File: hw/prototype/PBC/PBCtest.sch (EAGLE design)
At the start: 180 parts, among them IC1 7812L, U1 TC4427EOA, U10 TC4427EOA, U11 TC4427EOA, U12 TC4427EOA, U13 TC4427EOA, U14 TC4427EOA, U15 TC4427EOA, U16 TC4427EOA, U17 TC4427EOA, U18 TC4427EOA, U19 TC4427EOA, U2 TC4427EOA, U20 TC4427EOA, U21 TC4427EOA, U22 TC4427EOA, U23 TC4427EOA, U24 TC4427EOA, U25 TC4427EOA, U26 TC4427EOA, U27 TC4427EOA, U28 TC4427EOA, U29 TC4427EOA, U3 TC4427EOA, U30 TC4427EOA, U31 TC4427EOA, U32 TC4427EOA, U4 TC4427EOA, U5 TC4427EOA, U6 TC4427EOA, U7 TC4427EOA, U8 TC4427EOA, U9 TC4427EOA

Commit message: schematic done
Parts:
- removed C10, C11, C12, C13, C14, C15, C16, C17, C18, C19, C2, C20, C21, C22, C23, C24, C25, C26, C27, C28, C29, C3, C30, C31, C32, C34, C35, C36, C37, C38, C39, C4, C40, C41, C42, C43, C44, C45, C46, C47, C48, C49, C5, C50, C51, C52, C53, C54, C55, C56, C57, C58, C59, C6, C60, C61, C62, C63, C64, C7, C8, C9: 2.2uF, rcl:C-EUC1206
- removed RESET: (no value), switch-omron:10-XX
- removed SVI1, SVI2, SVI5, SVI6, SVO1, SVO2, SVO4, SVO5, SVO6: (no value), con-lstb:MA08-1
- removed SVI3, SVO3: (no value), con-lstb:MA10-1
- removed SVI7: (no value), con-lstb:MA18-2
- removed U$1, U$10, U$11, U$12, U$13, U$14, U$15, U$16, U$17, U$18, U$19, U$2, U$20, U$21, U$22, U$23, U$24, U$25, U$26, U$27, U$28, U$29, U$30, U$31, U$32, U$33, U$34, U$35, U$36, U$37, U$38, U$39, U$40, U$41, U$42, U$43, U$44, U$45, U$46, U$47, U$48, U$49, U$5, U$50, U$51, U$52, U$53, U$54, U$55, U$56, U$57, U$58, U$59, U$6, U$60, U$61, U$62, U$63, U$64, U$7, U$8, U$9: (no value), ultrasonic:TCT40-16
- removed U10, U11, U12, U13, U14, U15, U16, U17, U18, U19, U2, U20, U21, U22, U23, U24, U25, U26, U27, U28, U29, U3, U30, U31, U32, U4, U5, U6, U7, U8, U9: TC4427EOA, TC4427EOA:TC4427EOA
- added S1: (no value), switch-omron:10-XX
- C65, C66: value 100pF -> (none)
- D1: value 1N4001 -> 1N4004
- renumbered PWR_IN to J1, SVI4 to SVI10, VIN_ENABLE to SVJ8
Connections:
- removed net +18V: C1.1, C10.1, C11.1, C12.1, C13.1, C14.1, C15.1, C16.1, C17.1, C18.1, C19.1, C2.1, C20.1, C21.1, C22.1, C23.1, C24.1, C25.1, C26.1, C27.1, C28.1, C29.1, C3.1, C30.1, C31.1, C32.1, C33.1, C34.1, C35.1, C36.1, C37.1, C38.1, C39.1, C4.1, C40.1, C41.1, C42.1, C43.1, C44.1, C45.1, C46.1, C47.1, C48.1, C49.1, C5.1, C50.1, C51.1, C52.1, C53.1, C54.1, C55.1, C56.1, C57.1, C58.1, C59.1, C6.1, C60.1, C61.1, C62.1, C63.1, C64.1, C65.1, C7.1, C8.1, C9.1, D1.C, IC1.VI, U1.VDD, U10.VDD, U11.VDD, U12.VDD, U13.VDD, U14.VDD, U15.VDD, U16.VDD, U17.VDD, U18.VDD, U19.VDD, U2.VDD, U20.VDD, U21.VDD, U22.VDD, U23.VDD, U24.VDD, U25.VDD, U26.VDD, U27.VDD, U28.VDD, U29.VDD, U3.VDD, U30.VDD, U31.VDD, U32.VDD, U4.VDD, U5.VDD, U6.VDD, U7.VDD, U8.VDD, U9.VDD
- removed net +3V3: SVI10.5, SVO4.5
- removed net +5V: SVI10.4, SVI7.1, SVI7.2, SVO4.4
- removed net AREF: SVI3.8, SVO3.8
- removed net IOREF: SVI10.7, SVO4.7
- removed net PA0: SVI2.1, SVO2.1
- removed net PA1: SVI2.2, SVO2.2
- removed net PA10: SVI3.3, SVO3.3, U3.IN_A
- removed net PA11: SVI3.4, SVO3.4, U3.IN_B
- removed net PA12: SVI3.5, SVO3.5, U4.IN_A
- removed net PA13: SVI3.6, SVO3.6, U4.IN_B
- removed net PA14: SVI1.8, SVO1.8, U5.IN_A
- removed net PA15: SVI1.7, SVO1.7, U5.IN_B
- removed net PA16: SVI1.6, SVO1.6, U6.IN_A
- removed net PA17: SVI1.5, SVO1.5, U6.IN_B
- removed net PA18: SVI1.4, SVO1.4, U7.IN_A
- removed net PA19: SVI1.3, SVO1.3, U7.IN_B
- removed net PA2: SVI2.3, SVO2.3
- removed net PA20: SVI1.2, SVO1.2, U8.IN_A
- removed net PA21: SVI1.1, SVO1.1, U8.IN_B
- removed net PA22: SVI7.3, U9.IN_A
- removed net PA23: SVI7.4, U10.IN_A
- removed net PA24: SVI7.5, U9.IN_B
- removed net PA25: SVI7.6, U10.IN_B
- removed net PA26: SVI7.7, U11.IN_A
- removed net PA27: SVI7.8, U12.IN_A
- removed net PA28: SVI7.9, U11.IN_B
- removed net PA29: SVI7.10, U12.IN_B
- removed net PA3: SVI2.4, SVO2.4
- removed net PA30: SVI7.11, U13.IN_A
- removed net PA31: SVI7.12, U14.IN_A
- removed net PA32: SVI7.13, U13.IN_B
- removed net PA33: SVI7.14, U14.IN_B
- removed net PA34: SVI7.15, U15.IN_A
- removed net PA35: SVI7.16, U16.IN_A
- removed net PA36: SVI7.17, U15.IN_B
- removed net PA37: SVI7.18, U16.IN_B
- removed net PA38: SVI7.19, U17.IN_A
- removed net PA39: SVI7.20, U18.IN_A
- removed net PA4: SVI2.5, SVO2.5
- removed net PA40: SVI7.21, U17.IN_B
- removed net PA41: SVI7.22, U18.IN_B
- removed net PA42: SVI7.23, U19.IN_A
- removed net PA43: SVI7.24, U20.IN_A
- removed net PA44: SVI7.25, U19.IN_B
- removed net PA45: SVI7.26, U20.IN_B
- removed net PA46: SVI7.27, U21.IN_A
- removed net PA47: SVI7.28, U22.IN_A
- removed net PA48: SVI7.29, U21.IN_B
- removed net PA49: SVI7.30, U22.IN_B
- removed net PA5: SVI2.6, SVO2.6
- removed net PA50: SVI7.31, U23.IN_A
- removed net PA51: SVI7.32, U24.IN_A
- removed net PA52: SVI7.33, U23.IN_B
- removed net PA53: SVI7.34, U24.IN_B
- removed net PA54: SVI5.8, SVO5.8, U25.IN_A
- removed net PA55: SVI5.7, SVO5.7, U25.IN_B
- removed net PA56: SVI5.6, SVO5.6, U26.IN_A
- removed net PA57: SVI5.5, SVO5.5, U26.IN_B
- removed net PA58: SVI5.4, SVO5.4, U27.IN_A
- removed net PA59: SVI5.3, SVO5.3, U27.IN_B
- removed net PA60: SVI5.2, SVO5.2, U28.IN_A
- removed net PA61: SVI5.1, SVO5.1, U28.IN_B
- removed net PA62: SVI6.8, SVO6.8, U29.IN_A
- removed net PA63: SVI6.7, SVO6.7, U29.IN_B
- removed net PA64: SVI6.6, SVO6.6, U30.IN_A
- removed net PA65: SVI6.5, SVO6.5, U30.IN_B
- removed net PA66: SVI6.4, SVO6.4, U31.IN_A
- removed net PA67: SVI6.3, SVO6.3, U31.IN_B
- removed net PA68: SVI6.2, SVO6.2, U32.IN_A
- removed net PA69: SVI6.1, SVO6.1, U32.IN_B
- removed net PA8: SVI3.1, SVO3.1, U2.IN_A
- removed net PA9: SVI3.2, SVO3.2, U2.IN_B
- removed net PD10: U$8.P0, U3.!OUT_A
- removed net PD11: U$7.P0, U3.!OUT_B
- removed net PD12: U$10.P0, U4.!OUT_A
- removed net PD13: U$9.P0, U4.!OUT_B
- removed net PD14: U$2.P0, U5.!OUT_A
- removed net PD15: U$1.P0, U5.!OUT_B
- removed net PD16: U$12.P0, U6.!OUT_A
- removed net PD17: U$11.P0, U6.!OUT_B
- removed net PD18: U$14.P0, U7.!OUT_A
- removed net PD19: U$13.P0, U7.!OUT_B
- removed net PD20: U$16.P0, U8.!OUT_A
- removed net PD21: U$15.P0, U8.!OUT_B
- removed net PD22: U$18.P0, U9.!OUT_A
- removed net PD23: U$20.P0, U10.!OUT_A
- removed net PD24: U$17.P0, U9.!OUT_B
- removed net PD25: U$19.P0, U10.!OUT_B
- removed net PD26: U$22.P0, U11.!OUT_A
- removed net PD27: U$24.P0, U12.!OUT_A
- removed net PD28: U$21.P0, U11.!OUT_B
- removed net PD29: U$23.P0, U12.!OUT_B
- removed net PD30: U$26.P0, U13.!OUT_A
- removed net PD31: U$28.P0, U14.!OUT_A
- removed net PD32: U$25.P0, U13.!OUT_B
- removed net PD33: U$27.P0, U14.!OUT_B
- removed net PD34: U$30.P0, U15.!OUT_A
- removed net PD35: U$32.P0, U16.!OUT_A
- removed net PD36: U$29.P0, U15.!OUT_B
- removed net PD37: U$31.P0, U16.!OUT_B
- removed net PD38: U$34.P0, U17.!OUT_A
- removed net PD39: U$36.P0, U18.!OUT_A
- removed net PD40: U$33.P0, U17.!OUT_B
- removed net PD41: U$35.P0, U18.!OUT_B
- removed net PD42: U$38.P0, U19.!OUT_A
- removed net PD43: U$40.P0, U20.!OUT_A
- removed net PD44: U$37.P0, U19.!OUT_B
- removed net PD45: U$39.P0, U20.!OUT_B
- removed net PD46: U$42.P0, U21.!OUT_A
- removed net PD47: U$44.P0, U22.!OUT_A
- removed net PD48: U$41.P0, U21.!OUT_B
- removed net PD49: U$43.P0, U22.!OUT_B
- removed net PD50: U$46.P0, U23.!OUT_A
- removed net PD51: U$48.P0, U24.!OUT_A
- removed net PD52: U$45.P0, U23.!OUT_B
- removed net PD53: U$47.P0, U24.!OUT_B
- removed net PD54: U$50.P0, U25.!OUT_A
- removed net PD55: U$49.P0, U25.!OUT_B
- removed net PD56: U$52.P0, U26.!OUT_A
- removed net PD57: U$51.P0, U26.!OUT_B
- removed net PD58: U$54.P0, U27.!OUT_A
- removed net PD59: U$53.P0, U27.!OUT_B
- removed net PD60: U$56.P0, U28.!OUT_A
- removed net PD61: U$55.P0, U28.!OUT_B
- removed net PD62: U$58.P0, U29.!OUT_A
- removed net PD63: U$57.P0, U29.!OUT_B
- removed net PD64: U$60.P0, U30.!OUT_A
- removed net PD65: U$59.P0, U30.!OUT_B
- removed net PD66: U$62.P0, U31.!OUT_A
- removed net PD67: U$61.P0, U31.!OUT_B
- removed net PD68: U$64.P0, U32.!OUT_A
- removed net PD69: U$63.P0, U32.!OUT_B
- removed net PD8: U$6.P0, U2.!OUT_A
- removed net PD9: U$5.P0, U2.!OUT_B
- removed net SCL: SVI3.10, SVO3.10
- removed net SDA: SVI3.9, SVO3.9
- new net 5V: SVI10.4
- new net V20: C1.1, C33.1, C65.1, D1.C, IC1.VI, U1.VDD
- net GND: now also S1.S, S1.S1; no longer C10.2, C11.2, C12.2, C13.2, C14.2, C15.2, C16.2, C17.2, C18.2, C19.2, C2.2, C20.2, C21.2, C22.2, C23.2, C24.2, C25.2, C26.2, C27.2, C28.2, C29.2, C3.2, C30.2, C31.2, C32.2, C34.2, C35.2, C36.2, C37.2, C38.2, C39.2, C4.2, C40.2, C41.2, C42.2, C43.2, C44.2, C45.2, C46.2, C47.2, C48.2, C49.2, C5.2, C50.2, C51.2, C52.2, C53.2, C54.2, C55.2, C56.2, C57.2, C58.2, C59.2, C6.2, C60.2, C61.2, C62.2, C63.2, C64.2, C7.2, C8.2, C9.2, RESET.S, RESET.S1, SVI3.7, SVI7.35, SVI7.36, SVO3.7, SVO4.2, SVO4.3, U$1.P1, U$10.P1, U$11.P1, U$12.P1, U$13.P1, U$14.P1, U$15.P1, U$16.P1, U$17.P1, U$18.P1, U$19.P1, U$2.P1, U$20.P1, U$21.P1, U$22.P1, U$23.P1, U$24.P1, U$25.P1, U$26.P1, U$27.P1, U$28.P1, U$29.P1, U$30.P1, U$31.P1, U$32.P1, U$33.P1, U$34.P1, U$35.P1, U$36.P1, U$37.P1, U$38.P1, U$39.P1, U$40.P1, U$41.P1, U$42.P1, U$43.P1, U$44.P1, U$45.P1, U$46.P1, U$47.P1, U$48.P1, U$49.P1, U$5.P1, U$50.P1, U$51.P1, U$52.P1, U$53.P1, U$54.P1, U$55.P1, U$56.P1, U$57.P1, U$58.P1, U$59.P1, U$6.P1, U$60.P1, U$61.P1, U$62.P1, U$63.P1, U$64.P1, U$7.P1, U$8.P1, U$9.P1, U10.GND, U11.GND, U12.GND, U13.GND, U14.GND, U15.GND, U16.GND, U17.GND, U18.GND, U19.GND, U2.GND, U20.GND, U21.GND, U22.GND, U23.GND, U24.GND, U25.GND, U26.GND, U27.GND, U28.GND, U29.GND, U3.GND, U30.GND, U31.GND, U32.GND, U4.GND, U5.GND, U6.GND, U7.GND, U8.GND, U9.GND
- net PA6: now also SVI10.7; no longer SVI2.7, SVO2.7
- net PA7: now also SVI10.8; no longer SVI2.8, SVO2.8
- net RESET: now also S1.P, S1.P1; no longer RESET.P, RESET.P1, SVO4.6
- net VIN: no longer SVJ8.3, SVO4.1

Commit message: tracing
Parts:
- renumbered U$3 to T1, U$4 to T2
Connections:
- net PA6: now also U1.IN_B; no longer U1.IN_A
- net PA7: now also U1.IN_A; no longer U1.IN_B
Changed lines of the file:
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@@
 <part name="V4" library="supply1" library_urn="urn:adsk.eagle:library:371" deviceset="VCC" device="" value="V20"/>
 <part name="GND9" library="supply1" library_urn="urn:adsk.eagle:library:371" deviceset="GND" device=""/>
-<part name="U$3" library="ultrasonic" deviceset="TCT40-16" device=""/>
-<part name="U$4" library="ultrasonic" deviceset="TCT40-16" device=""/>
+<part name="T1" library="ultrasonic" deviceset="TCT40-16" device=""/>
+<part name="T2" library="ultrasonic" deviceset="TCT40-16" device=""/>
 <part name="C1" library="rcl" library_urn="urn:adsk.eagle:library:334" deviceset="C-EU" device="C1206" package3d_urn="urn:adsk.eagle:package:23618/2" value="2.2uF"/>
 <part name="C33" library="rcl" library_urn="urn:adsk.eagle:library:334" deviceset="C-EU" device="C1206" package3d_urn="urn:adsk.eagle:package:23618/2" value="2.2uF"/>
@@
 <attribute name="VALUE" x="198.12" y="111.76" size="1.778" layer="96"/>
 </instance>
-<instance part="U$3" gate="G$1" x="220.98" y="121.92" smashed="yes" rot="MR0">
+<instance part="T1" gate="G$1" x="220.98" y="121.92" smashed="yes" rot="MR0">
 <attribute name="NAME" x="219.71" y="119.38" size="1.27" layer="95" rot="MR0"/>
 <attribute name="VALUE" x="219.71" y="116.84" size="1.27" layer="96" rot="MR0"/>
 </instance>
-<instance part="U$4" gate="G$1" x="220.98" y="137.16" smashed="yes" rot="MR0">
+<instance part="T2" gate="G$1" x="220.98" y="137.16" smashed="yes" rot="MR0">
 <attribute name="NAME" x="219.71" y="134.62" size="1.27" layer="95" rot="MR0"/>
 <attribute name="VALUE" x="219.71" y="132.08" size="1.27" layer="96" rot="MR0"/>
@@
 <net name="PA6" class="0">
 <segment>
+<wire x1="15.24" y1="55.88" x2="27.94" y2="55.88" width="0.1524" layer="91"/>
+<label x="17.78" y="55.88" size="1.778" layer="95"/>
+<pinref part="SVI10" gate="1" pin="7"/>
+</segment>
+<segment>
+<pinref part="U1" gate="A" pin="IN_B"/>
+<wire x1="160.02" y1="132.08" x2="144.78" y2="132.08" width="0.1524" layer="91"/>
+<label x="147.32" y="132.08" size="1.778" layer="95"/>
+</segment>
+</net>
+<net name="PA7" class="0">
+<segment>
+<pinref part="SVI10" gate="1" pin="8"/>
+<wire x1="15.24" y1="58.42" x2="27.94" y2="58.42" width="0.1524" layer="91"/>
+<label x="17.78" y="58.42" size="1.778" layer="95"/>
+</segment>
+<segment>
 <pinref part="U1" gate="A" pin="IN_A"/>
 <wire x1="160.02" y1="134.62" x2="144.78" y2="134.62" width="0.1524" layer="91"/>
 <label x="147.32" y="134.62" size="1.778" layer="95"/>
-</segment>
-<segment>
-<wire x1="15.24" y1="55.88" x2="27.94" y2="55.88" width="0.1524" layer="91"/>
-<label x="17.78" y="55.88" size="1.778" layer="95"/>
-<pinref part="SVI10" gate="1" pin="7"/>
-</segment>
-</net>
-<net name="PA7" class="0">
-<segment>
-<pinref part="U1" gate="A" pin="IN_B"/>
-<wire x1="160.02" y1="132.08" x2="144.78" y2="132.08" width="0.1524" layer="91"/>
-<label x="147.32" y="132.08" size="1.778" layer="95"/>
-</segment>
-<segment>
-<pinref part="SVI10" gate="1" pin="8"/>
-<wire x1="15.24" y1="58.42" x2="27.94" y2="58.42" width="0.1524" layer="91"/>
-<label x="17.78" y="58.42" size="1.778" layer="95"/>
 </segment>
 </net>
@@
 <label x="203.2" y="121.92" size="1.778" layer="95"/>
 <pinref part="GND9" gate="1" pin="GND"/>
-<pinref part="U$4" gate="G$1" pin="P1"/>
+<pinref part="T2" gate="G$1" pin="P1"/>
 <wire x1="215.9" y1="137.16" x2="213.36" y2="137.16" width="0.1524" layer="91"/>
 <wire x1="213.36" y1="137.16" x2="213.36" y2="121.92" width="0.1524" layer="91"/>
 <wire x1="213.36" y1="121.92" x2="200.66" y2="121.92" width="0.1524" layer="91"/>
-<pinref part="U$3" gate="G$1" pin="P1"/>
+<pinref part="T1" gate="G$1" pin="P1"/>
 <wire x1="215.9" y1="121.92" x2="213.36" y2="121.92" width="0.1524" layer="91"/>
 <junction x="213.36" y="121.92"/>
@@
 <wire x1="195.58" y1="134.62" x2="210.82" y2="134.62" width="0.1524" layer="91"/>
 <wire x1="210.82" y1="134.62" x2="210.82" y2="139.7" width="0.1524" layer="91"/>
-<pinref part="U$4" gate="G$1" pin="P0"/>
+<pinref part="T2" gate="G$1" pin="P0"/>
 <wire x1="210.82" y1="139.7" x2="215.9" y2="139.7" width="0.1524" layer="91"/>
 <label x="200.66" y="134.62" size="1.778" layer="95"/>
@@
 <wire x1="195.58" y1="132.08" x2="210.82" y2="132.08" width="0.1524" layer="91"/>
 <wire x1="210.82" y1="132.08" x2="210.82" y2="124.46" width="0.1524" layer="91"/>
-<pinref part="U$3" gate="G$1" pin="P0"/>
+<pinref part="T1" gate="G$1" pin="P0"/>
 <wire x1="210.82" y1="124.46" x2="215.9" y2="124.46" width="0.1524" layer="91"/>
 <label x="200.66" y="132.08" size="1.778" layer="95"/>

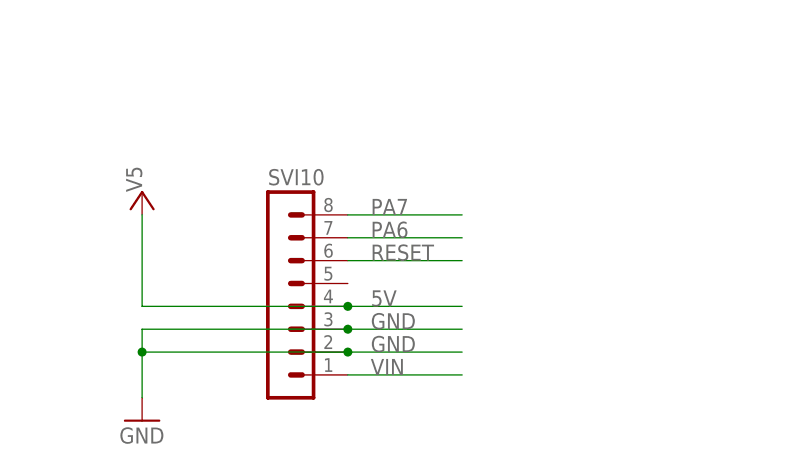
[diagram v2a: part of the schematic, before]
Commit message: Board design enhancments
* New alignment marks
* Increased thermal isolation to 20mil
* Upgraded PCBtest to new design rules with 20mil clearance and increased text size to test the same object sizes of the main board
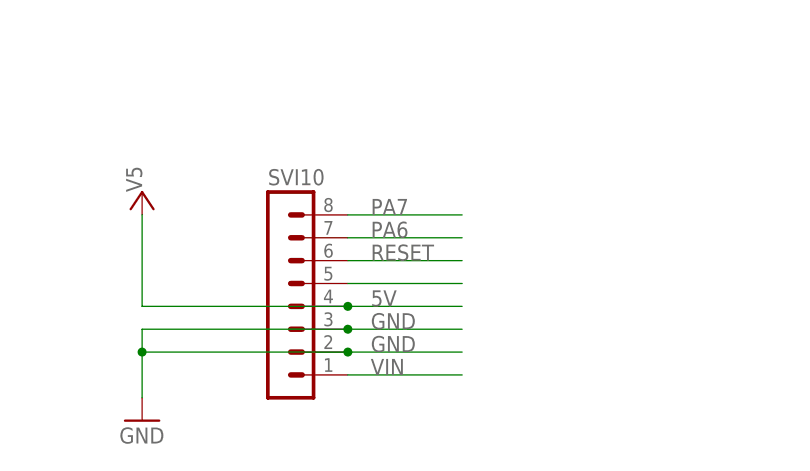
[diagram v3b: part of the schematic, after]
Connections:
- new net N$2: SVI10.5
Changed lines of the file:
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@@
+</segment>
+</net>
+<net name="N$2" class="0">
+<segment>
+<pinref part="SVI10" gate="1" pin="5"/>
+<wire x1="15.24" y1="50.8" x2="27.94" y2="50.8" width="0.1524" layer="91"/>
 </segment>
 </net>
